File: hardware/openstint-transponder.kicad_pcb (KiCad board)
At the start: 4 copper layers, 18.5 x 16 mm, 32 parts, among them J1 V+, J2 V-, Q1 AO3401A, U1 STM32C011F4Ux, U3 UCC27517DBV, U4 TLV760xx, Y1 20 MHz

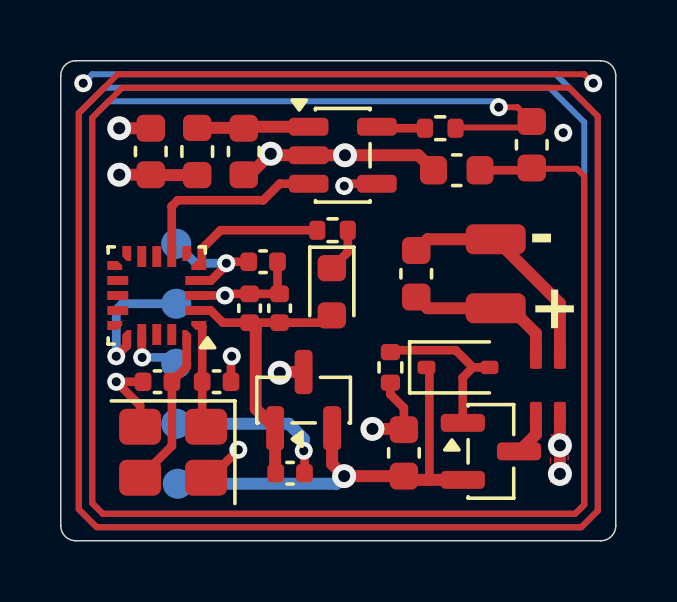
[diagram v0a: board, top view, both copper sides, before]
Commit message: antenna re-tuned
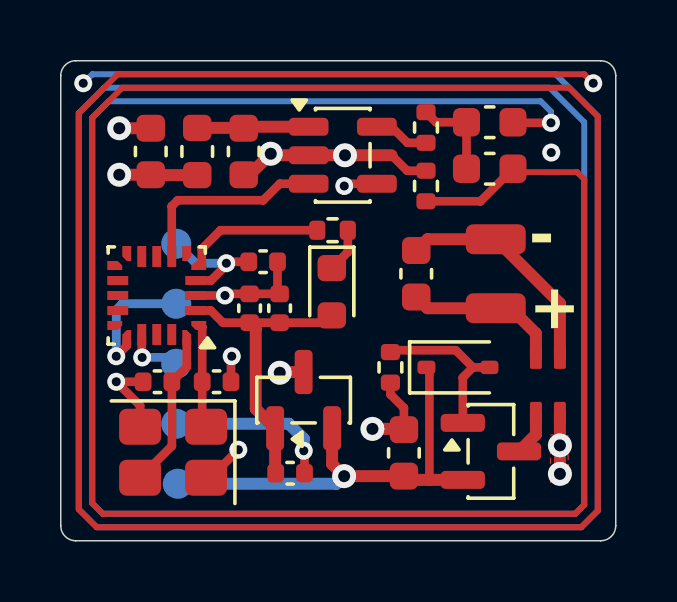
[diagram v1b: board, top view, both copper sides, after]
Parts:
- added R3: 0, Resistor_SMD:R_0402_1005Metric, F.Cu at (106.7, 103.7)
- C11: value 560p/NP0 -> 680p
- C6: value 750p/NP0 -> 470p
- moved C6 1.94 mm to (108.8, 101.5)
- moved C11 1.61 mm to (108.8, 103.1), turned to 0 degrees
- moved R2 0.48 mm to (106.7, 101.7), turned to 90 degrees
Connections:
- C11 pad 1: /ANTENNA_LOOP -> Net-(C11-Pad1)
- C6 pad 2: GND -> Net-(C11-Pad1)
- R2 pad 2: /ANTENNA_LOOP -> Net-(C11-Pad1)
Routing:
- net Net-(C11-Pad1): track 0.00 -> 3.04 mm
- net /ANTENNA_LOOP: track 5.69 -> 4.62 mm

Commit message: v2 transponder
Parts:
- removed D2: 9.1V, Diode_SMD:D_SOD-323
- removed L1: 68n, Inductor_SMD:L_0603_1608Metric
- removed TP5: TestPoint, TestPoint:TestPoint_Pad_D1.0mm
- removed U4: TLV760xx, Package_TO_SOT_SMD:SOT-23
- removed Y1: 20 MHz, Crystal:Crystal_SMD_3225-4Pin_3.2x2.5mm
- added C13: 22p, Capacitor_SMD:C_0402_1005Metric, F.Cu at (132.6, 104.7)
- added C14: 22p, Capacitor_SMD:C_0402_1005Metric, F.Cu at (132.6, 100.1)
- added C15: 10u, Capacitor_SMD:C_0402_1005Metric, F.Cu at (132.7, 106.0)
- added L2: 3.3u, Inductor_SMD:L_0603_1608Metric, F.Cu at (130.9, 104.9)
- added L3: 3.3u, Inductor_SMD:L_0603_1608Metric, F.Cu at (130.9, 99.9)
- added R4: 22, Resistor_SMD:R_0402_1005Metric, F.Cu at (130.9, 97.4)
- added R6: 100k, Resistor_SMD:R_0402_1005Metric, F.Cu at (135.2, 105.4)
- added R7: 100k, Resistor_SMD:R_0402_1005Metric, F.Cu at (135.7, 108.8)
- added U2: 10 MHz, Crystal:Crystal_SMD_3225-4Pin_3.2x2.5mm, F.Cu at (144.7, 106.8)
- C1: value 4.7u/16V -> 10u; footprint Capacitor_SMD:C_0603_1608Metric -> Capacitor_SMD:C_0402_1005Metric
- C10: value 4.7u/16V -> 100n; footprint Capacitor_SMD:C_0603_1608Metric -> Capacitor_SMD:C_0402_1005Metric
- C11: value 680p -> 1n; footprint Capacitor_SMD:C_0603_1608Metric -> Capacitor_SMD:C_0402_1005Metric
- C4: value 20p -> 100n
- C5: value 20p -> 10n
- C6: value 470p -> 1n; footprint Capacitor_SMD:C_0603_1608Metric -> Capacitor_SMD:C_0402_1005Metric
- Q1: value AO3401A -> PMGD280UN; footprint Package_TO_SOT_SMD:SOT-23 -> Package_TO_SOT_SMD:SOT-363_SC-70-6
- R1: value 220 -> 22
- R3: value 0 -> 22
- U1: value STM32C011F4Ux -> ATtiny1616-M; footprint Package_DFN_QFN:ST_UFQFPN-20_3x3mm_P0.5mm -> Package_DFN_QFN:VQFN-20-1EP_3x3mm_P0.4mm_EP1.7x1.7mm
- U3: value UCC27517DBV -> SPX3819M5-L-3-3
- moved TP3 50.3 mm to (145.9, 97.0), turned to 90 degrees
- moved TP4 49.1 mm to (145.9, 99.6), turned to 90 degrees
- moved TP1 47.7 mm to (145.9, 102.1), turned to 90 degrees
- moved TP2 47.7 mm to (145.9, 104.7), turned to 180 degrees
- moved C4 44.7 mm to (142.3, 108.0), turned to -90 degrees
- moved U1 41.2 mm to (138.9, 107.7), turned to -90 degrees
- moved C7 38.7 mm to (141.3, 96.9)
- moved C5 38.0 mm to (135.1, 96.5)
- moved C3 37.8 mm to (138.5, 104.8), turned to 180 degrees
- moved C12 36.9 mm to (138.5, 103.8), turned to 0 degrees
- moved R5 36.5 mm to (140.0, 102.5), turned to 90 degrees
- moved J1 36.2 mm to (143.9, 98.2)
- moved C9 36.0 mm to (135.2, 98.9), turned to -90 degrees
- moved FL1 35.9 mm to (143.7, 96.2), turned to 180 degrees
- moved C8 35.6 mm to (141.3, 99.9), turned to -90 degrees
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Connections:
- C1 pad 1: /V_PUSHPULL -> +3.3V
- C10 pad 1: VDDA -> GND
- C10 pad 2: GND -> +3.3V
- C11 pad 1: Net-(C11-Pad1) -> /A+
- C11 pad 2: /ANTENNA_LOOP -> /A-
- C2 pad 1: /~{RST} -> GND
- C2 pad 2: GND -> +3.3V
- C4 pad 2: Net-(U1-PC14) -> +3.3V
- C5 pad 1: GND -> Net-(U3-BP)
- C5 pad 2: Net-(U1-PC15) -> GND
- C6 pad 1: /ANTENNA_LOOP -> /A+
- C6 pad 2: Net-(C11-Pad1) -> /A-
- FL1 pad 1: /VIN- -> /VIN+
- FL1 pad 2: /VIN+ -> /VIN-
- FL1 pad 3: /VFILT+ -> GND
- FL1 pad 4: GND -> VDDA
- Q1 pad 1: /revpol_gate -> GND
- Q1 pad 2: VDDA -> /GANT+
- Q1 pad 3: /VFILT+ -> /A-
- R1 pad 1: GND -> /ANT+
- R1 pad 2: /revpol_gate -> /GANT+
- R2 pad 1: Net-(U3-OUT) -> /GANT-
- R2 pad 2: Net-(C11-Pad1) -> /ANT-
- R3 pad 1: GND -> Net-(L2-Pad1)
- R3 pad 2: /ANTENNA_LOOP -> +3.3V
- TP1 pad 1: /~{RST} -> /UDPI
- TP2 pad 1: /SWDIO -> /UART0TXD
- U1 pad 1: Net-(U1-PC15) -> unconnected-(U1-PA2-Pad1)
- U1 pad 16: /SWDIO -> unconnected-(U1-PC1-Pad16)
- U1 pad 17: /SWCLK -> unconnected-(U1-PC2-Pad17)
- U1 pad 19: unconnected-(U1-PB7-Pad19) -> /UDPI
- U1 pad 2: +3.3V -> /EXTCLK
- U1 pad 20: Net-(U1-PC14) -> /UART0TXD
- U1 pad 4: /~{RST} -> +3.3V
- U1 pad 5: /~{BLINKY} -> /ANT+
- U1 pad 6: unconnected-(U1-PA1-Pad6) -> /~{BLINKY}
- U1 pad 7: /ANT_IN -> unconnected-(U1-PA6-Pad7)
- U1 pad 8: unconnected-(U1-PA3-Pad8) -> /ANT-
- U3 pad 1: /V_PUSHPULL -> VDDA
- U3 pad 3: /ANT_IN -> VDDA
- U3 pad 4: GND -> Net-(U3-BP)
- U3 pad 5: Net-(U3-OUT) -> +3.3V
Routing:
- net GND: track 44.2 -> 78.9 mm, vias 13 -> 6
- net +3.3V: track 10.2 -> 43.8 mm, vias 0 -> 5
- net VDDA: track 32.6 -> 16.2 mm
- net /A-: track 0.00 -> 9.25 mm, vias 0 -> 3
- net /GANT-: track 0.00 -> 9.20 mm, vias 0 -> 2
- net /UDPI: track 0.00 -> 7.81 mm, vias 0 -> 2
- net /UART0TXD: track 0.00 -> 7.00 mm, vias 0 -> 2
- net /ANT_IN: track 6.55 -> 0.00 mm
- net /A+: track 0.00 -> 5.69 mm, vias 0 -> 1
- net /EXTCLK: track 0.00 -> 5.57 mm
- net /revpol_gate: track 5.55 -> 0.00 mm
- net /~{BLINKY}: track 4.67 -> 10.0 mm, vias 0 -> 2
- net Net-(U1-PC14): track 5.24 -> 0.00 mm
- net /ANTENNA_LOOP: track 4.62 -> 0.00 mm, vias 4 -> 0
- net /SWDIO: track 4.33 -> 0.00 mm, vias 1 -> 0
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- removed copper zone on F.Cu, net GND
- removed copper zone on In1.Cu, net GND
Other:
- board size 18.5 x 16 mm -> 18 x 15 mm
- board text added: "TxD"
- board text added: "UDPI"
- board text added: "VDD"
- board text removed: "CLK"
- board text removed: "DIO"
- board text removed: "RST"
- board text removed: "VCC"

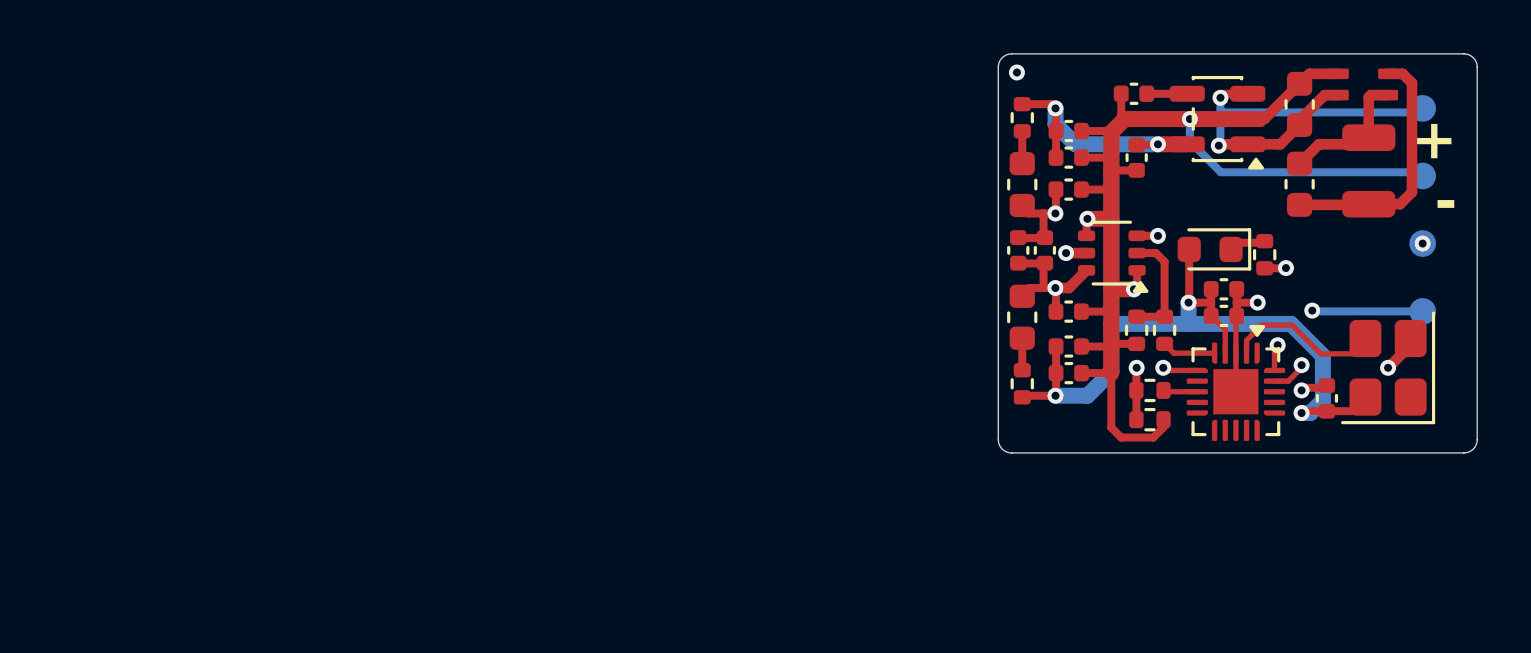
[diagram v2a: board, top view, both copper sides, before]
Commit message: Revert "v2 transponder"
This reverts commit ef6581161f0553e0c47b9335515ce2e00a666ec4.
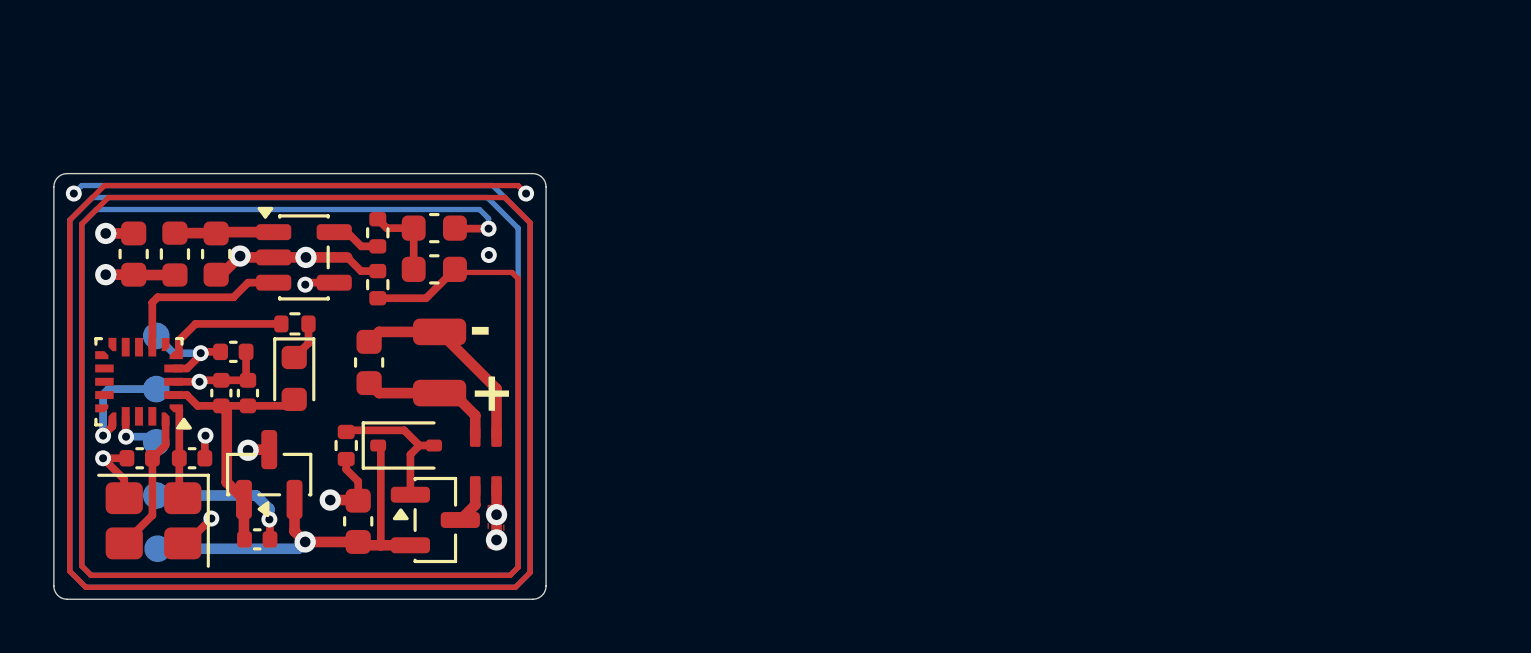
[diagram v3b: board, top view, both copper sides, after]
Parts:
- removed C13, C14: 22p, Capacitor_SMD:C_0402_1005Metric
- removed C15: 10u, Capacitor_SMD:C_0402_1005Metric
- removed L2, L3: 3.3u, Inductor_SMD:L_0603_1608Metric
- removed R4: 22, Resistor_SMD:R_0402_1005Metric
- removed R6, R7: 100k, Resistor_SMD:R_0402_1005Metric
- removed U2: 10 MHz, Crystal:Crystal_SMD_3225-4Pin_3.2x2.5mm
- added D2: 9.1V, Diode_SMD:D_SOD-323, F.Cu at (107.7, 109.7)
- added L1: 68n, Inductor_SMD:L_0603_1608Metric, F.Cu at (99.0, 102.5)
- added TP5: TestPoint, TestPoint:TestPoint_Pad_D1.0mm, B.Cu at (98.3, 109.6)
- added U4: TLV760xx, Package_TO_SOT_SMD:SOT-23, F.Cu at (102.6, 110.8)
- added Y1: 20 MHz, Crystal:Crystal_SMD_3225-4Pin_3.2x2.5mm, F.Cu at (98.2, 112.5)
- C1: value 10u -> 4.7u/16V; footprint Capacitor_SMD:C_0402_1005Metric -> Capacitor_SMD:C_0603_1608Metric
- C10: value 100n -> 4.7u/16V; footprint Capacitor_SMD:C_0402_1005Metric -> Capacitor_SMD:C_0603_1608Metric
- C11: value 1n -> 680p; footprint Capacitor_SMD:C_0402_1005Metric -> Capacitor_SMD:C_0603_1608Metric
- C4: value 100n -> 20p
- C5: value 10n -> 20p
- C6: value 1n -> 470p; footprint Capacitor_SMD:C_0402_1005Metric -> Capacitor_SMD:C_0603_1608Metric
- Q1: value PMGD280UN -> AO3401A; footprint Package_TO_SOT_SMD:SOT-363_SC-70-6 -> Package_TO_SOT_SMD:SOT-23
- R1: value 22 -> 220
- R3: value 22 -> 0
- U1: value ATtiny1616-M -> STM32C011F4Ux; footprint Package_DFN_QFN:VQFN-20-1EP_3x3mm_P0.4mm_EP1.7x1.7mm -> Package_DFN_QFN:ST_UFQFPN-20_3x3mm_P0.5mm
- U3: value SPX3819M5-L-3-3 -> UCC27517DBV
- moved TP3 50.3 mm to (98.4, 113.6), turned to 0 degrees
- moved TP4 49.1 mm to (98.3, 111.6), turned to 0 degrees
- moved TP1 47.7 mm to (98.3, 105.6), turned to 0 degrees
- moved TP2 47.7 mm to (98.3, 107.6), turned to 0 degrees
- moved C4 44.7 mm to (97.7, 110.2), turned to 0 degrees
- moved U1 41.2 mm to (97.7, 107.3), turned to 180 degrees
- moved C7 38.7 mm to (105.9, 112.6)
- moved C5 38.0 mm to (99.7, 110.2)
- moved C3 37.8 mm to (100.8, 107.8), turned to -90 degrees
- moved C12 36.9 mm to (101.8, 107.8), turned to 90 degrees
- moved R5 36.5 mm to (103.6, 105.2), turned to 0 degrees
- moved J1 36.2 mm to (109.0, 107.8)
- moved C9 36.0 mm to (102.1, 113.2), turned to 0 degrees
- moved FL1 35.9 mm to (110.7, 110.3), turned to -90 degrees
- moved C8 35.6 mm to (106.3, 106.6), turned to 90 degrees
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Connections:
- C1 pad 1: +3.3V -> /V_PUSHPULL
- C10 pad 1: GND -> VDDA
- C10 pad 2: +3.3V -> GND
- C11 pad 1: /A+ -> Net-(C11-Pad1)
- C11 pad 2: /A- -> /ANTENNA_LOOP
- C2 pad 1: GND -> /~{RST}
- C2 pad 2: +3.3V -> GND
- C4 pad 2: +3.3V -> Net-(U1-PC14)
- C5 pad 1: Net-(U3-BP) -> GND
- C5 pad 2: GND -> Net-(U1-PC15)
- C6 pad 1: /A+ -> /ANTENNA_LOOP
- C6 pad 2: /A- -> Net-(C11-Pad1)
- FL1 pad 1: /VIN+ -> /VIN-
- FL1 pad 2: /VIN- -> /VIN+
- FL1 pad 3: GND -> /VFILT+
- FL1 pad 4: VDDA -> GND
- Q1 pad 1: GND -> /revpol_gate
- Q1 pad 2: /GANT+ -> VDDA
- Q1 pad 3: /A- -> /VFILT+
- R1 pad 1: /ANT+ -> GND
- R1 pad 2: /GANT+ -> /revpol_gate
- R2 pad 1: /GANT- -> Net-(U3-OUT)
- R2 pad 2: /ANT- -> Net-(C11-Pad1)
- R3 pad 1: Net-(L2-Pad1) -> GND
- R3 pad 2: +3.3V -> /ANTENNA_LOOP
- TP1 pad 1: /UDPI -> /~{RST}
- TP2 pad 1: /UART0TXD -> /SWDIO
- U1 pad 1: unconnected-(U1-PA2-Pad1) -> Net-(U1-PC15)
- U1 pad 16: unconnected-(U1-PC1-Pad16) -> /SWDIO
- U1 pad 17: unconnected-(U1-PC2-Pad17) -> /SWCLK
- U1 pad 19: /UDPI -> unconnected-(U1-PB7-Pad19)
- U1 pad 2: /EXTCLK -> +3.3V
- U1 pad 20: /UART0TXD -> Net-(U1-PC14)
- U1 pad 4: +3.3V -> /~{RST}
- U1 pad 5: /ANT+ -> /~{BLINKY}
- U1 pad 6: /~{BLINKY} -> unconnected-(U1-PA1-Pad6)
- U1 pad 7: unconnected-(U1-PA6-Pad7) -> /ANT_IN
- U1 pad 8: /ANT- -> unconnected-(U1-PA3-Pad8)
- U3 pad 1: VDDA -> /V_PUSHPULL
- U3 pad 3: VDDA -> /ANT_IN
- U3 pad 4: Net-(U3-BP) -> GND
- U3 pad 5: +3.3V -> Net-(U3-OUT)
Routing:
- net GND: track 78.9 -> 44.2 mm, vias 6 -> 13
- net +3.3V: track 43.8 -> 10.2 mm, vias 5 -> 0
- net VDDA: track 16.2 -> 32.6 mm
- net /A-: track 9.25 -> 0.00 mm, vias 3 -> 0
- net /GANT-: track 9.20 -> 0.00 mm, vias 2 -> 0
- net /UDPI: track 7.81 -> 0.00 mm, vias 2 -> 0
- net /UART0TXD: track 7.00 -> 0.00 mm, vias 2 -> 0
- net /ANT_IN: track 0.00 -> 6.55 mm
- net /A+: track 5.69 -> 0.00 mm, vias 1 -> 0
- net /EXTCLK: track 5.57 -> 0.00 mm
- net /revpol_gate: track 0.00 -> 5.55 mm
- net /~{BLINKY}: track 10.0 -> 4.67 mm, vias 2 -> 0
- net Net-(U1-PC14): track 0.00 -> 5.24 mm
- net /ANTENNA_LOOP: track 0.00 -> 4.62 mm, vias 0 -> 4
- net /SWDIO: track 0.00 -> 4.33 mm, vias 0 -> 1
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- added copper zone on F.Cu, net GND
- added copper zone on In1.Cu, net GND
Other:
- board size 18 x 15 mm -> 18.5 x 16 mm
- board text added: "CLK"
- board text added: "DIO"
- board text added: "RST"
- board text added: "VCC"
- board text removed: "TxD"
- board text removed: "UDPI"
- board text removed: "VDD"
